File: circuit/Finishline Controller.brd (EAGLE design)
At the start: 99.1 x 53.3 mm, 23 parts, among them IC1 74HCT245N, IC2 MAX3490ESA

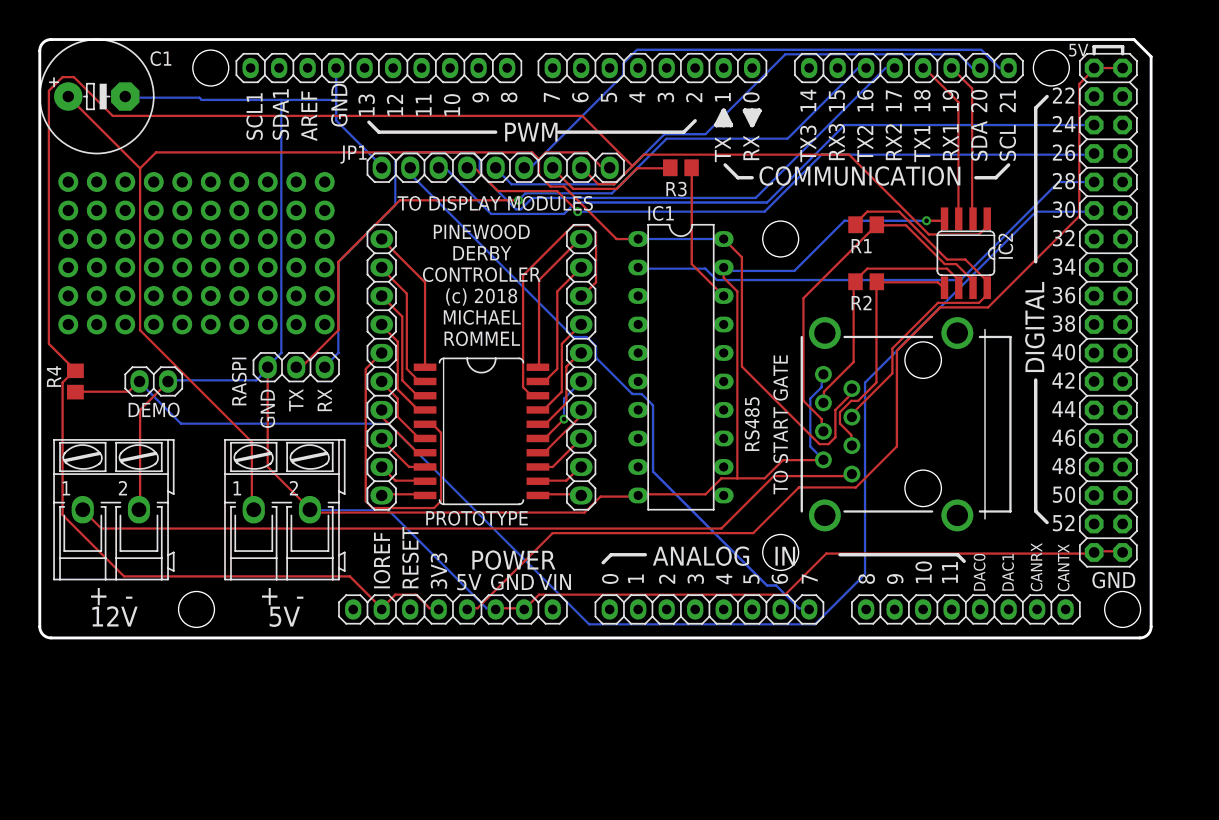
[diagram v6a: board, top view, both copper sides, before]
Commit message: create the final schematics and boards
Some schematics errors have been corrected. Another connector for
the laser diodes of the Finishing Gate has been added. The
connectors to the daughterboards have been rotated, so that the
cabling will run mostly straight.

All gerber files have been added as well as .zip files for the
boardhouse.
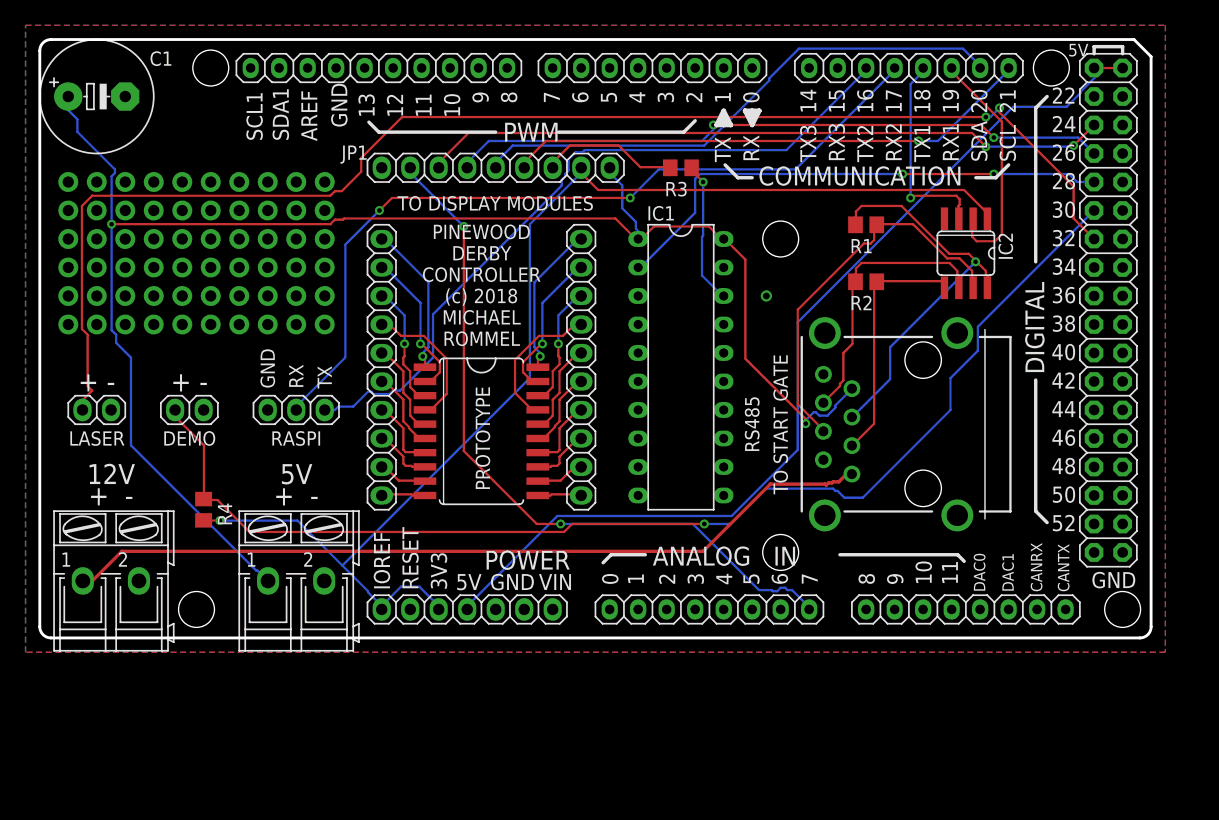
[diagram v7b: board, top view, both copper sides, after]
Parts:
- added JP6: lASER, pinhead:1X02
- POWER: value 8x1F-H8.5 -> POWER; device SmartPrj:1X08 -> pinhead:1X07
- moved R4 16.2 mm to (14.6, 11.4), turned to 270 degrees
- moved 5V 6.48 mm to (22.9, 5.08)
- moved 12V 6.35 mm to (6.35, 5.08)
- moved JP2 4.07 mm to (13.3, 20.3)
- moved JP3 3.81 mm to (22.9, 20.3)
- moved POWER 1.27 mm to (38.1, 2.54)
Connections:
- net +3V3: now also POWER.1, POWER.3; no longer POWER.2, POWER.4
- net +5V: now also POWER.4; no longer POWER.5
- net GND: now also JP6.2, POWER.5; no longer POWER.7
- net MASTER-RESET: now also POWER.2; no longer POWER.3
- net PIN32: now also JP6.1
- net RX2: now also JP3.2; no longer JP3.1
- net TX2: now also JP3.1; no longer JP3.2
- net VIN: now also POWER.7; no longer POWER.8
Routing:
- net GND: track 266.1 -> 0.00 mm
- net PIN32: track 0.00 -> 120.3 mm, vias 0 -> 2
- net +3V3: track 175.1 -> 109.1 mm, vias 0 -> 1
- net N$82: track 28.9 -> 8.48 mm
- net PIN30: track 125.4 -> 105.1 mm, vias 0 -> 1
- net N$89: track 26.5 -> 11.1 mm, vias 0 -> 1
- net AD7: track 56.3 -> 64.2 mm, vias 0 -> 2
- net RX1: track 14.2 -> 21.4 mm
- net +5V: track 90.4 -> 85.9 mm
- net +5VEXT: track 136.0 -> 140.3 mm, vias 0 -> 2
- net TX1: track 14.8 -> 18.4 mm, vias 0 -> 1
- net N$90: track 9.52 -> 12.8 mm
- net N$81: track 9.58 -> 12.7 mm
- net PIN24: track 63.4 -> 61.3 mm, vias 0 -> 2
- net RX2: track 73.8 -> 72.2 mm, vias 0 -> 2
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- added copper zone on layer 1, net GND
- added copper zone on layer 16, net GND
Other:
- board text added: "LASER"
